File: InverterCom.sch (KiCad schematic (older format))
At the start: 3 parts, among them U8 SN65HVD230

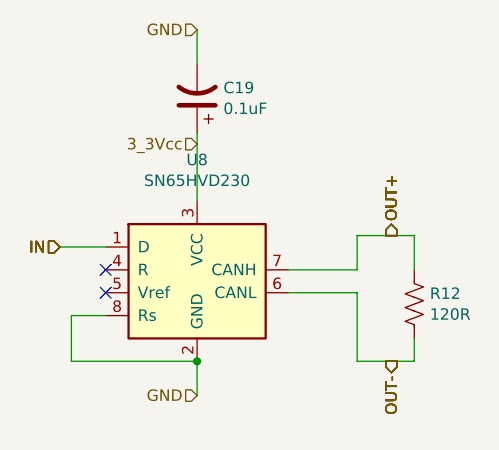
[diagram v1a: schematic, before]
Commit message: 4 layer board that passes checks
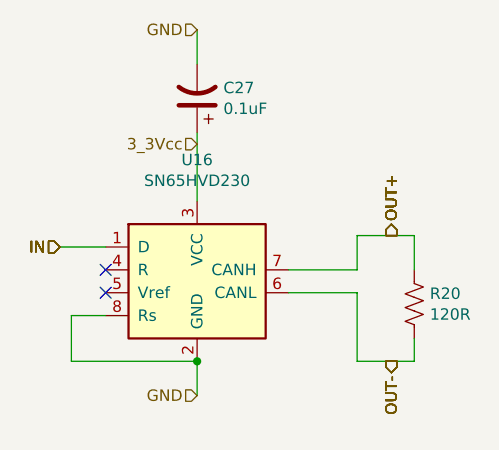
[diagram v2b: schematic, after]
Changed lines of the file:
@@
 $Descr A4 11693 8268
 encoding utf-8
-Sheet 4 37
+Sheet 4 36
 Title ""
 Date ""
@@
 AR Path="/603BF418/604500E5" Ref="U?"  Part="1"
 AR Path="/603BF7FF/604500E5" Ref="U16"  Part="1"
-F 0 "U8" H 5850 3981 50  0000 C CNN
+F 0 "U16" H 5850 3981 50  0000 C CNN
 F 1 "SN65HVD230" H 5850 3890 50  0000 C CNN
 F 2 "Package_SO:SOIC-8_3.9x4.9mm_P1.27mm" H 5850 3000 50  0001 C CNN
@@
 AR Path="/603BF418/604500E6" Ref="R?"  Part="1"
 AR Path="/603BF7FF/604500E6" Ref="R20"  Part="1"
-F 0 "R12" H 6868 3696 50  0000 L CNN
+F 0 "R20" H 6868 3696 50  0000 L CNN
 F 1 "120R" H 6868 3605 50  0000 L CNN
 F 2 "Resistor_SMD:R_0805_2012Metric" V 6840 3640 50  0001 C CNN
@@
 AR Path="/603BF418/603C009E" Ref="C?"  Part="1"
 AR Path="/603BF7FF/603C009E" Ref="C27"  Part="1"
-F 0 "C19" H 5735 2704 50  0000 R CNN
+F 0 "C27" H 5735 2704 50  0000 R CNN
 F 1 "0.1uF" H 5735 2795 50  0000 R CNN
 F 2 "Capacitor_SMD:C_0805_2012Metric" H 5850 2750 50  0001 C CNN

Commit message: Routed PCB
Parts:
- C19: JLCPCB_PN (none) -> C49678
- R12: JLCPCB_PN (none) -> C17437
- U8: JLCPCB_PN (none) -> C12084
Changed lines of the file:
@@
 AR Path="/603BF418/604500E5" Ref="U?"  Part="1"
 AR Path="/603BF7FF/604500E5" Ref="U16"  Part="1"
-F 0 "U16" H 5850 3981 50  0000 C CNN
+F 0 "U8" H 5850 3981 50  0000 C CNN
 F 1 "SN65HVD230" H 5850 3890 50  0000 C CNN
 F 2 "Package_SO:SOIC-8_3.9x4.9mm_P1.27mm" H 5850 3000 50  0001 C CNN
 F 3 "http://www.ti.com/lit/ds/symlink/sn65hvd230.pdf" H 5750 3900 50  0001 C CNN
+F 4 "C12084" H 5850 3500 50  0001 C CNN "JLCPCB_PN"
 	1    5850 3500
 	1    0    0    -1
@@
 AR Path="/603BF418/604500E6" Ref="R?"  Part="1"
 AR Path="/603BF7FF/604500E6" Ref="R20"  Part="1"
-F 0 "R20" H 6868 3696 50  0000 L CNN
+F 0 "R12" H 6868 3696 50  0000 L CNN
 F 1 "120R" H 6868 3605 50  0000 L CNN
 F 2 "Resistor_SMD:R_0805_2012Metric" V 6840 3640 50  0001 C CNN
 F 3 "~" H 6800 3650 50  0001 C CNN
+F 4 "C17437" H 6800 3650 50  0001 C CNN "JLCPCB_PN"
 	1    6800 3650
 	1    0    0    -1
@@
 AR Path="/603BF418/603C009E" Ref="C?"  Part="1"
 AR Path="/603BF7FF/603C009E" Ref="C27"  Part="1"
-F 0 "C27" H 5735 2704 50  0000 R CNN
+F 0 "C19" H 5735 2704 50  0000 R CNN
 F 1 "0.1uF" H 5735 2795 50  0000 R CNN
 F 2 "Capacitor_SMD:C_0805_2012Metric" H 5850 2750 50  0001 C CNN
 F 3 "~" H 5850 2750 50  0001 C CNN
+F 4 "C49678" H 5850 2750 50  0001 C CNN "JLCPCB_PN"
 	1    5850 2750
 	-1   0    0    1

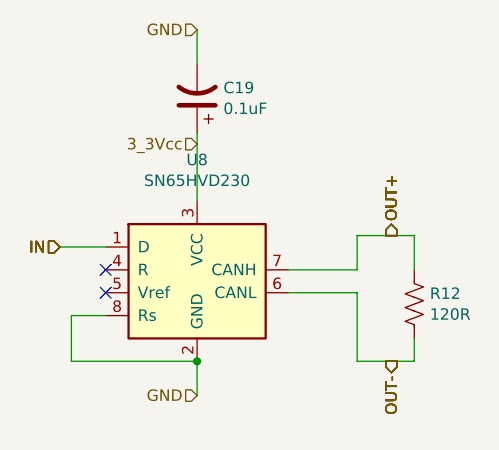
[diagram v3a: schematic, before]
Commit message: Checkpoint 2022-01-19
Design with bluepill to run the heater since we lose some of the SPI
pins to the USB port on the STM32-H107.
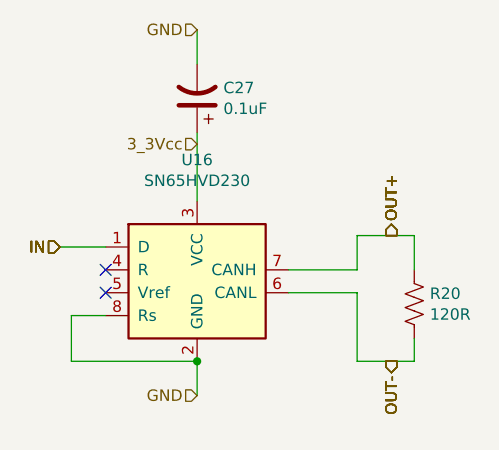
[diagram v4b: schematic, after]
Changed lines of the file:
@@
 $Descr A4 11693 8268
 encoding utf-8
-Sheet 4 36
+Sheet 4 37
 Title ""
 Date ""
@@
 AR Path="/603BF418/604500E5" Ref="U?"  Part="1"
 AR Path="/603BF7FF/604500E5" Ref="U16"  Part="1"
-F 0 "U8" H 5850 3981 50  0000 C CNN
+F 0 "U16" H 5850 3981 50  0000 C CNN
 F 1 "SN65HVD230" H 5850 3890 50  0000 C CNN
 F 2 "Package_SO:SOIC-8_3.9x4.9mm_P1.27mm" H 5850 3000 50  0001 C CNN
@@
 AR Path="/603BF418/604500E6" Ref="R?"  Part="1"
 AR Path="/603BF7FF/604500E6" Ref="R20"  Part="1"
-F 0 "R12" H 6868 3696 50  0000 L CNN
+F 0 "R20" H 6868 3696 50  0000 L CNN
 F 1 "120R" H 6868 3605 50  0000 L CNN
 F 2 "Resistor_SMD:R_0805_2012Metric" V 6840 3640 50  0001 C CNN
@@
 AR Path="/603BF418/603C009E" Ref="C?"  Part="1"
 AR Path="/603BF7FF/603C009E" Ref="C27"  Part="1"
-F 0 "C19" H 5735 2704 50  0000 R CNN
+F 0 "C27" H 5735 2704 50  0000 R CNN
 F 1 "0.1uF" H 5735 2795 50  0000 R CNN
 F 2 "Capacitor_SMD:C_0805_2012Metric" H 5850 2750 50  0001 C CNN
